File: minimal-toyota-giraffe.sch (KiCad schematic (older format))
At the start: 6 parts, among them J1 USB_A, J2 MOBILEEYE, J3 MOBILEEYE, P1 panda, U1 Power

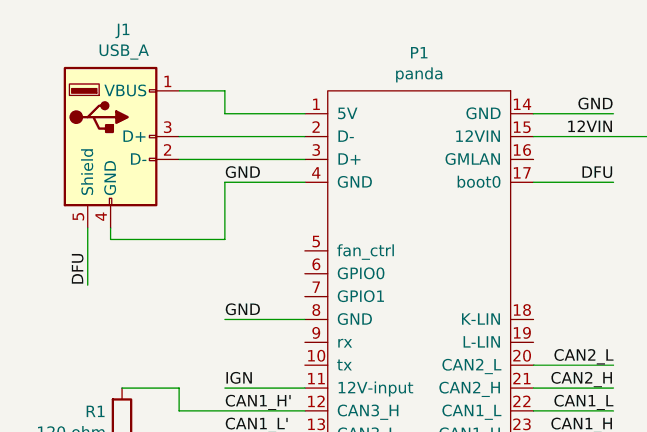
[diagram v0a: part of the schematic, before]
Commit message: fixed USB D+ D- flip
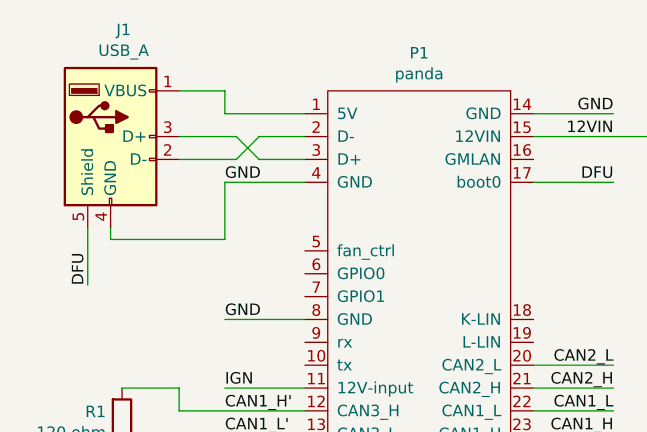
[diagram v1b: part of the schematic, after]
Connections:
- net at P1.2 (D-): now also J1.2 (D-); no longer J1.3 (D+)
- net at P1.3 (D+): now also J1.3 (D+); no longer J1.2 (D-)
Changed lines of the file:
@@
 EESchema Schematic File Version 4
+LIBS:minimal-toyota-giraffe-cache
 EELAYER 29 0
 EELAYER END
@@
 	2550 2500 2900 2500
 Wire Wire Line
-	2350 2600 2900 2600
-Wire Wire Line
-	2900 2700 2350 2700
-Wire Wire Line
 	2550 2800 2550 3050
 Wire Wire Line
@@
 Text Notes 4550 3000 0    50   ~ 0
 Const 12V\n-Comma Power\n-Mirror Pin\n-Sun Roof
+Wire Wire Line
+	2350 2700 2600 2700
+Wire Wire Line
+	2600 2700 2700 2600
+Wire Wire Line
+	2700 2600 2900 2600
+Wire Wire Line
+	2900 2700 2700 2700
+Wire Wire Line
+	2700 2700 2600 2600
+Wire Wire Line
+	2600 2600 2350 2600
 $EndSCHEMATC

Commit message: new board design
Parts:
- removed J1: USB_A, giraffe:USB, symbol Connector:USB_A
- added JP1: Paw_Boot, Jumper:SolderJumper-2_P1.3mm_Open_RoundedPad1.0x1.5mm, symbol Jumper:SolderJumper_2_Open
- added U2: USB, giraffe:USB, symbol giraffe:USB
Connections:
- net DFU: now also JP1.2 (B)
- net GND: now also U2.4 (GND)
- net at P1.1 (5V): now also JP1.1 (A), U2.1 (VCC)
- net at P1.2 (D-): now also U2.3 (D+)
- net at P1.3 (D+): now also U2.2 (D-)
- net 2: now reaches J2.2
- net 2: now also J3.2
- net 3: now reaches J2.3
- net 3: now also J3.3
- net 4: now reaches J2.4
- net 4: now also J3.4
- net 8: now reaches J2.8
- net 8: now also J3.8
- net 9: now reaches J2.9
- net 9: now also J3.9
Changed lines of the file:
@@
 Text Label 4250 2500 2    50   ~ 0
 GND
-Wire Wire Line
-	2900 3400 2550 3400
-Wire Wire Line
-	2900 2800 2550 2800
 Text Label 4250 3900 2    50   ~ 0
 CAN1_H
@@
 Text Label 5000 5200 0    50   ~ 0
 CAN2_H
-Text Label 2550 2800 0    50   ~ 0
-GND
 Text Label 2550 3400 0    50   ~ 0
 GND
@@
 Wire Wire Line
 	2350 3900 2900 3900
-$Comp
-L Connector:USB_A J1
-U 1 1 5D3B6FC7
-P 2050 2600
-F 0 "J1" H 2107 3067 50  0000 C CNN
-F 1 "USB_A" H 2107 2976 50  0000 C CNN
-F 2 "giraffe:USB" H 2200 2550 50  0001 C CNN
-F 3 " ~" H 2200 2550 50  0001 C CNN
-	1    2050 2600
-	1    0    0    -1
-$EndComp
-Wire Wire Line
-	2350 2400 2550 2400
-Wire Wire Line
-	2550 2400 2550 2500
-Wire Wire Line
-	2550 2500 2900 2500
-Wire Wire Line
-	2550 2800 2550 3050
-Wire Wire Line
-	2550 3050 2050 3050
-Wire Wire Line
-	2050 3050 2050 3000
-Wire Wire Line
-	1950 3000 1950 3250
 Wire Wire Line
 	3900 2800 4250 2800
 Text Label 4250 2800 2    50   ~ 0
-DFU
-Text Label 1950 3250 1    50   ~ 0
 DFU
 Text Label 2550 3700 0    50   ~ 0
@@
 L giraffe:Power U1
 U 1 1 5D3CE919
-P 4500 2550
-F 0 "U1" H 4687 2725 50  0000 C CNN
-F 1 "Power" H 4687 2634 50  0000 C CNN
-F 2 "giraffe:12VIN" H 4500 2550 50  0001 C CNN
-F 3 "" H 4500 2550 50  0001 C CNN
-	1    4500 2550
+P 4250 2550
+F 0 "U1" H 4437 2725 50  0001 C CNN
+F 1 "Power" H 4437 2634 50  0001 C CNN
+F 2 "giraffe:12VIN" H 4250 2550 50  0001 C CNN
+F 3 "" H 4250 2550 50  0001 C CNN
+	1    4250 2550
 	1    0    0    -1
 $EndComp
-Wire Wire Line
-	3900 2600 4500 2600
-Text Notes 4550 3000 0    50   ~ 0
+Text Notes 4650 2700 0    50   ~ 0
 Const 12V\n-Comma Power\n-Mirror Pin\n-Sun Roof
 Wire Wire Line
@@
 Wire Wire Line
 	2600 2600 2350 2600
+$Comp
+L giraffe:USB U2
+U 1 1 5D49EE3F
+P 2150 2400
+F 0 "U2" H 2208 2525 50  0000 C CNN
+F 1 "USB" H 2208 2434 50  0000 C CNN
+F 2 "giraffe:USB" H 2150 2400 50  0001 C CNN
+F 3 "" H 2150 2400 50  0001 C CNN
+	1    2150 2400
+	1    0    0    -1
+$EndComp
+Wire Wire Line
+	2850 4800 2500 4800
+Wire Wire Line
+	2850 4900 2500 4900
+Wire Wire Line
+	2850 5000 2500 5000
+Wire Wire Line
+	3950 4800 4300 4800
+Wire Wire Line
+	3950 4900 4300 4900
+Wire Wire Line
+	5350 4800 5000 4800
+Wire Wire Line
+	5350 4900 5000 4900
+Wire Wire Line
+	5350 5000 5000 5000
+Wire Wire Line
+	6450 4800 6800 4800
+Wire Wire Line
+	6450 4900 6800 4900
+Text Label 5000 4800 0    50   ~ 0
+2
+Text Label 5000 4900 0    50   ~ 0
+3
+Text Label 5000 5000 0    50   ~ 0
+4
+Text Label 2500 4800 0    50   ~ 0
+2
+Text Label 2500 4900 0    50   ~ 0
+3
+Text Label 2500 5000 0    50   ~ 0
+4
+Text Label 4300 4800 2    50   ~ 0
+8
+Text Label 4300 4900 2    50   ~ 0
+9
+Text Label 6800 4800 2    50   ~ 0
+8
+Text Label 6800 4900 2    50   ~ 0
+9
+$Comp
+L Jumper:SolderJumper_2_Open JP1
+U 1 1 5D4ABECF
+P 4400 2800
+F 0 "JP1" H 4400 2600 50  0001 C CNN
+F 1 "Paw_Boot" H 4400 2900 50  0000 C CNN
+F 2 "Jumper:SolderJumper-2_P1.3mm_Open_RoundedPad1.0x1.5mm" H 4400 2800 50  0001 C CNN
+F 3 "~" H 4400 2800 50  0001 C CNN
+	1    4400 2800
+	-1   0    0    1
+$EndComp
+Wire Wire Line
+	2350 2800 2900 2800
+Wire Wire Line
+	2900 3400 2550 3400
+Text Label 2550 2800 0    50   ~ 0
+GND
+Wire Wire Line
+	2350 2500 2650 2500
+Wire Wire Line
+	3900 2600 4250 2600
+Wire Wire Line
+	5500 2800 5500 2050
+Wire Wire Line
+	5500 2050 2650 2050
+Wire Wire Line
+	2650 2050 2650 2500
+Wire Wire Line
+	4550 2800 5500 2800
+Connection ~ 2650 2500
+Wire Wire Line
+	2650 2500 2900 2500
 $EndSCHEMATC
